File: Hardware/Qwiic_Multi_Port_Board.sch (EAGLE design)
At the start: 9 parts, among them J1 QWIIC_RIGHT_ANGLE, J2 QWIIC_RIGHT_ANGLE, J3 QWIIC_RIGHT_ANGLE, J4 QWIIC_RIGHT_ANGLE

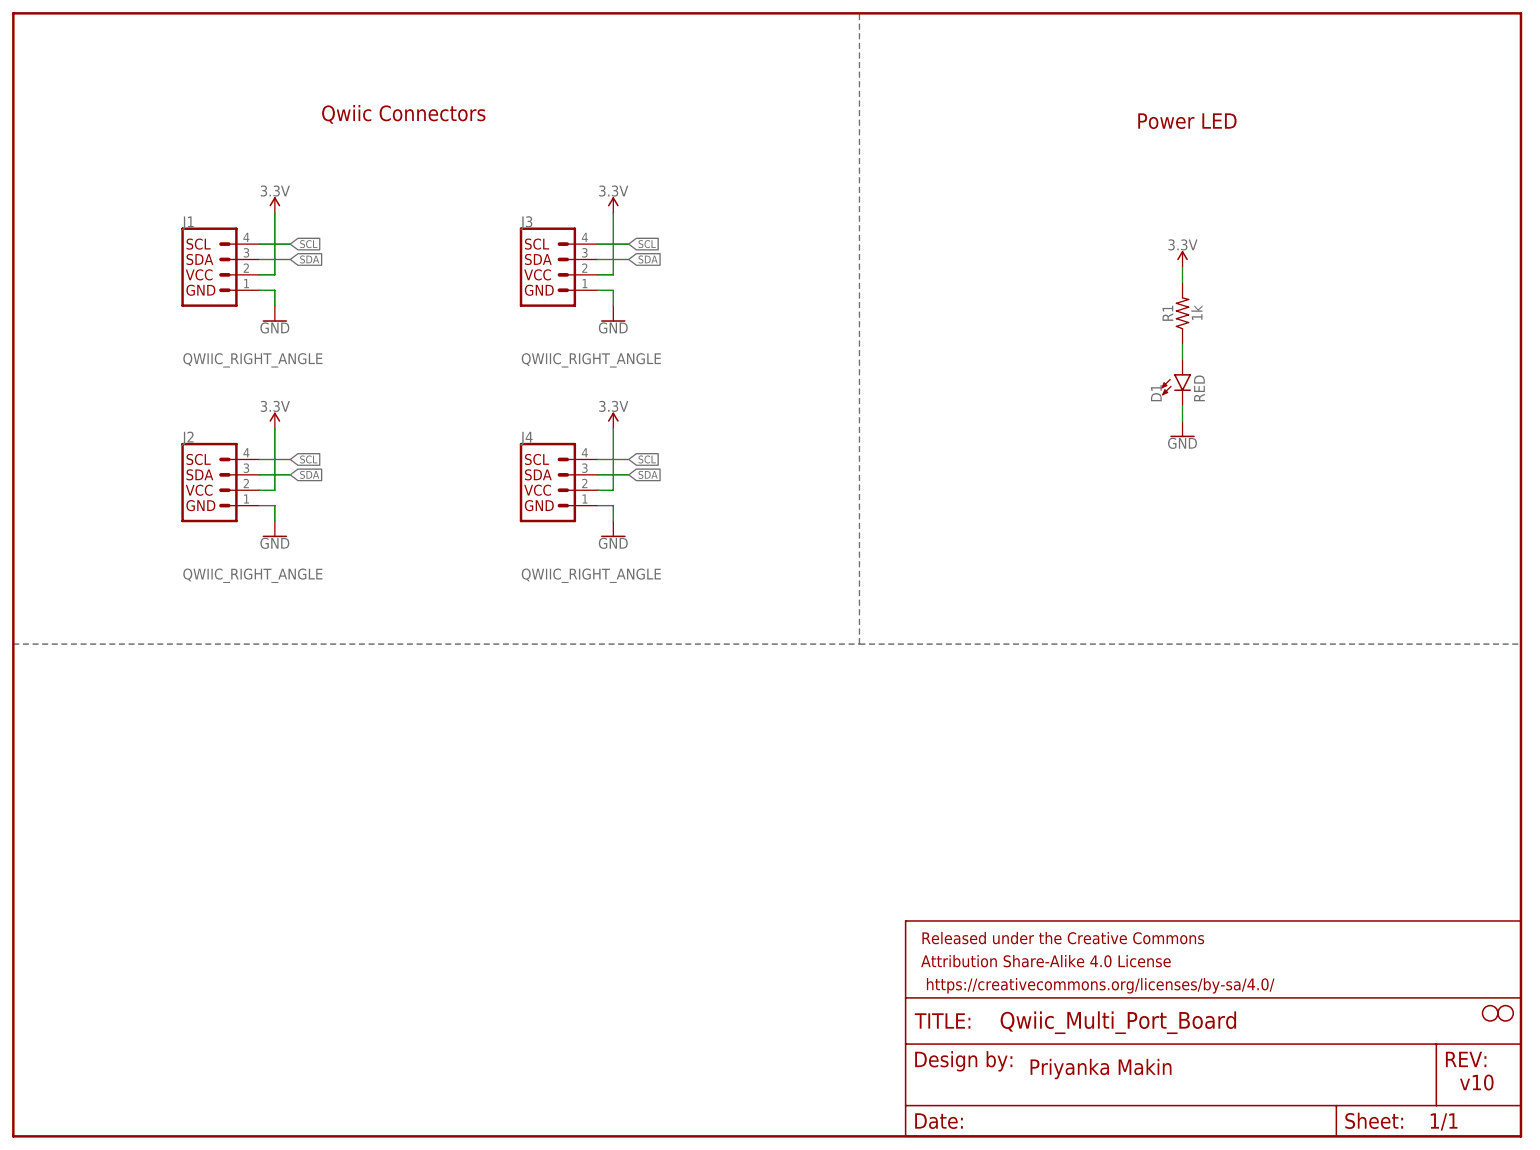
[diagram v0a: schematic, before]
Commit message: Multi Port: Design Review Changes
Added jumper on PWR LED
Added fiducials
Added OSHW, qwiic, SF logo as device on the schematic
Moved traces on top layer to avoid screws
Decided against:
un-populated I2C pullups -- not enough space
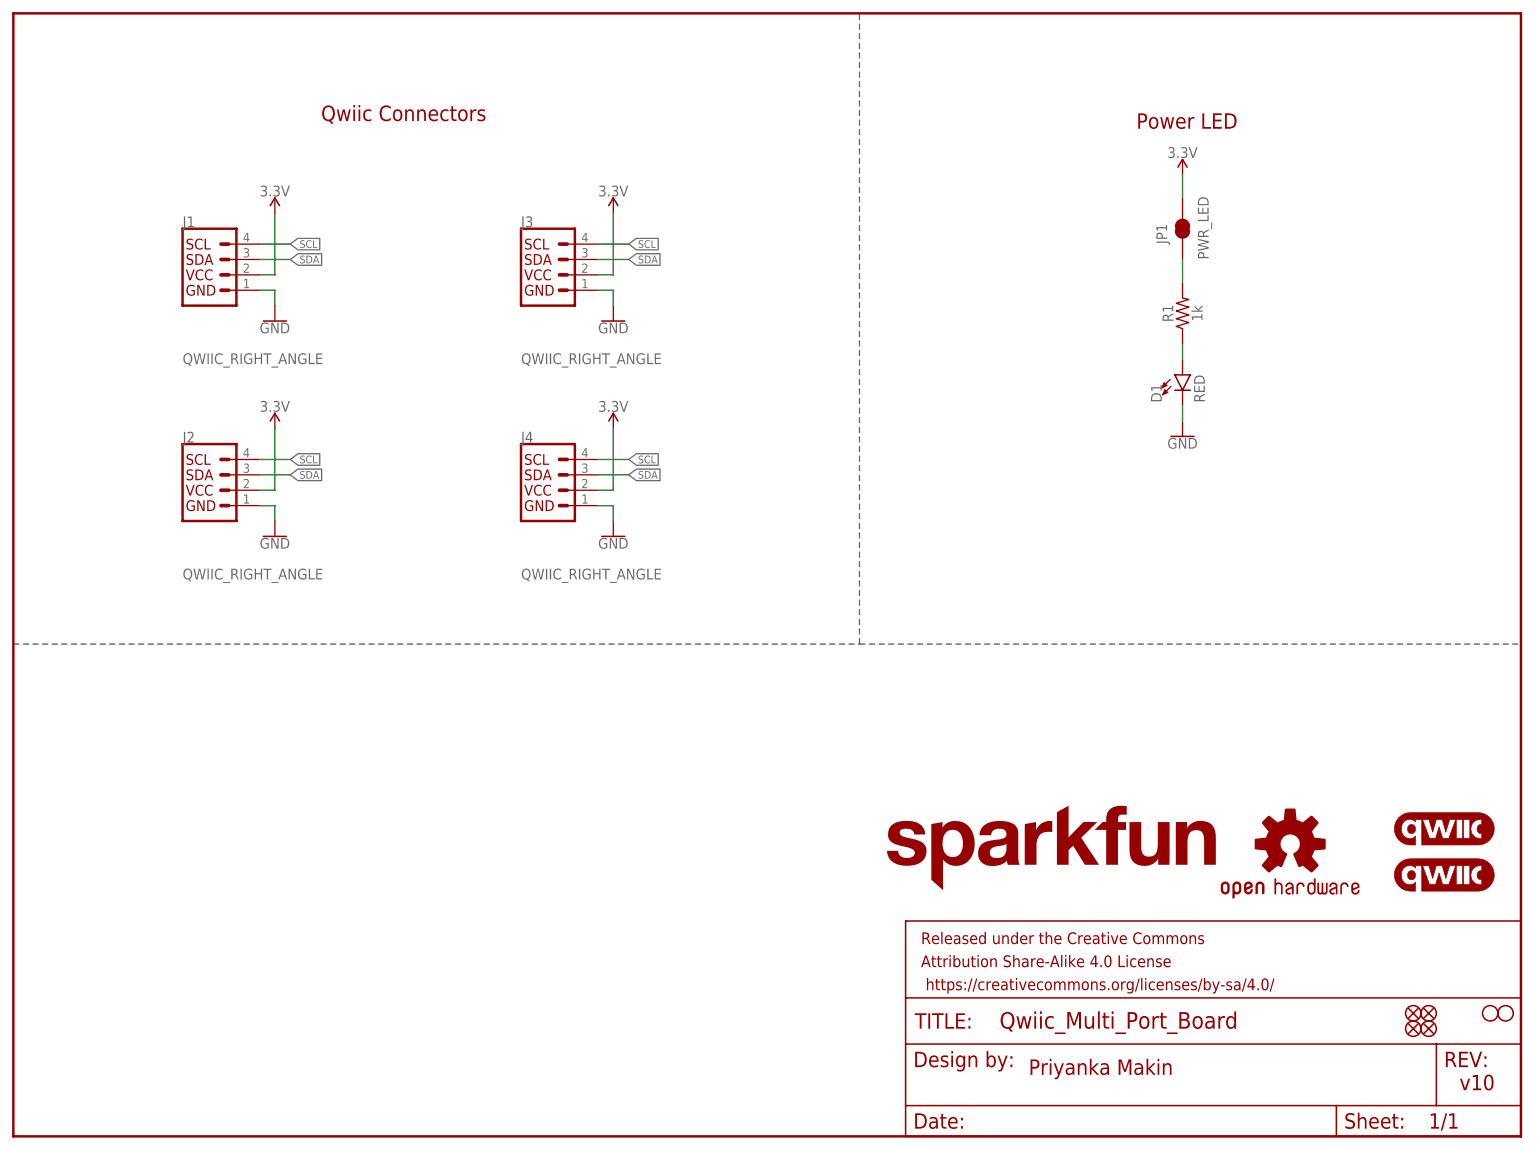
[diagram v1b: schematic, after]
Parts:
- added FD1, FD2, FD3, FD4: FIDUCIAL1X2, SparkFun-Aesthetics:FIDUCIAL1X2
- added JP1: PWR_LED, SparkFun-Jumpers:JUMPER-SMT_2_NC_TRACE_SILK
- added LOGO1, LOGO2: QWIIC_LOGO_5MM, SparkFun-Aesthetics:QWIIC_LOGO_5MM
- added LOGO3: OSHW-LOGOS, SparkFun-Aesthetics:OSHW-LOGOS
- added LOGO4: SFE_LOGO_NAME.2_INCH, SparkFun-Aesthetics:SFE_LOGO_NAME.2_INCH
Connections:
- new net N$2: JP1.1, R1.2
- net 3.3V: now also JP1.2; no longer R1.2

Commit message: Completed Engineering checklist
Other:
- note added: "Cut this jumper to disable the power LED"
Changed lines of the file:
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@@
 <grid distance="0.1" unitdist="inch" unit="inch" style="lines" multiple="1" display="no" altdistance="0.01" altunitdist="inch" altunit="inch"/>
 <layers>
-<layer number="1" name="Top" color="4" fill="1" visible="yes" active="no"/>
-<layer number="2" name="Route2" color="16" fill="1" visible="yes" active="no"/>
-<layer number="3" name="Route3" color="4" fill="3" visible="yes" active="no"/>
-<layer number="4" name="Route4" color="1" fill="4" visible="yes" active="no"/>
-<layer number="5" name="Route5" color="4" fill="4" visible="yes" active="no"/>
-<layer number="6" name="Route6" color="1" fill="8" visible="yes" active="no"/>
-<layer number="7" name="Route7" color="4" fill="8" visible="yes" active="no"/>
-<layer number="8" name="Route8" color="1" fill="2" visible="yes" active="no"/>
-<layer number="9" name="Route9" color="4" fill="2" visible="yes" active="no"/>
-<layer number="10" name="Route10" color="1" fill="7" visible="yes" active="no"/>
-<layer number="11" name="Route11" color="4" fill="7" visible="yes" active="no"/>
-<layer number="12" name="Route12" color="1" fill="5" visible="yes" active="no"/>
-<layer number="13" name="Route13" color="4" fill="5" visible="yes" active="no"/>
-<layer number="14" name="Route14" color="1" fill="6" visible="yes" active="no"/>
-<layer number="15" name="Route15" color="23" fill="1" visible="yes" active="no"/>
-<layer number="16" name="Bottom" color="1" fill="1" visible="yes" active="no"/>
-<layer number="17" name="Pads" color="2" fill="1" visible="yes" active="no"/>
-<layer number="18" name="Vias" color="2" fill="1" visible="yes" active="no"/>
-<layer number="19" name="Unrouted" color="6" fill="1" visible="yes" active="no"/>
-<layer number="20" name="Dimension" color="24" fill="1" visible="yes" active="no"/>
-<layer number="21" name="tPlace" color="16" fill="1" visible="yes" active="no"/>
-<layer number="22" name="bPlace" color="14" fill="1" visible="yes" active="no"/>
-<layer number="23" name="tOrigins" color="15" fill="1" visible="yes" active="no"/>
-<layer number="24" name="bOrigins" color="15" fill="1" visible="yes" active="no"/>
-<layer number="25" name="tNames" color="7" fill="1" visible="yes" active="no"/>
-<layer number="26" name="bNames" color="7" fill="1" visible="yes" active="no"/>
-<layer number="27" name="tValues" color="7" fill="1" visible="yes" active="no"/>
-<layer number="28" name="bValues" color="7" fill="1" visible="yes" active="no"/>
+<layer number="1" name="Top" color="4" fill="1" visible="no" active="no"/>
+<layer number="2" name="Route2" color="16" fill="1" visible="no" active="no"/>
+<layer number="3" name="Route3" color="4" fill="3" visible="no" active="no"/>
+<layer number="4" name="Route4" color="1" fill="4" visible="no" active="no"/>
+<layer number="5" name="Route5" color="4" fill="4" visible="no" active="no"/>
+<layer number="6" name="Route6" color="1" fill="8" visible="no" active="no"/>
+<layer number="7" name="Route7" color="4" fill="8" visible="no" active="no"/>
+<layer number="8" name="Route8" color="1" fill="2" visible="no" active="no"/>
+<layer number="9" name="Route9" color="4" fill="2" visible="no" active="no"/>
+<layer number="10" name="Route10" color="1" fill="7" visible="no" active="no"/>
+<layer number="11" name="Route11" color="4" fill="7" visible="no" active="no"/>
+<layer number="12" name="Route12" color="1" fill="5" visible="no" active="no"/>
+<layer number="13" name="Route13" color="4" fill="5" visible="no" active="no"/>
+<layer number="14" name="Route14" color="1" fill="6" visible="no" active="no"/>
+<layer number="15" name="Route15" color="23" fill="1" visible="no" active="no"/>
+<layer number="16" name="Bottom" color="1" fill="1" visible="no" active="no"/>
+<layer number="17" name="Pads" color="2" fill="1" visible="no" active="no"/>
+<layer number="18" name="Vias" color="2" fill="1" visible="no" active="no"/>
+<layer number="19" name="Unrouted" color="6" fill="1" visible="no" active="no"/>
+<layer number="20" name="Dimension" color="24" fill="1" visible="no" active="no"/>
+<layer number="21" name="tPlace" color="16" fill="1" visible="no" active="no"/>
+<layer number="22" name="bPlace" color="14" fill="1" visible="no" active="no"/>
+<layer number="23" name="tOrigins" color="15" fill="1" visible="no" active="no"/>
+<layer number="24" name="bOrigins" color="15" fill="1" visible="no" active="no"/>
+<layer number="25" name="tNames" color="7" fill="1" visible="no" active="no"/>
+<layer number="26" name="bNames" color="7" fill="1" visible="no" active="no"/>
+<layer number="27" name="tValues" color="7" fill="1" visible="no" active="no"/>
+<layer number="28" name="bValues" color="7" fill="1" visible="no" active="no"/>
 <layer number="29" name="tStop" color="7" fill="3" visible="no" active="no"/>
 <layer number="30" name="bStop" color="7" fill="6" visible="no" active="no"/>
@@
 <layer number="35" name="tGlue" color="7" fill="4" visible="no" active="no"/>
 <layer number="36" name="bGlue" color="7" fill="5" visible="no" active="no"/>
-<layer number="37" name="tTest" color="7" fill="1" visible="yes" active="no"/>
-<layer number="38" name="bTest" color="7" fill="1" visible="yes" active="no"/>
+<layer number="37" name="tTest" color="7" fill="1" visible="no" active="no"/>
+<layer number="38" name="bTest" color="7" fill="1" visible="no" active="no"/>
 <layer number="39" name="tKeepout" color="4" fill="11" visible="no" active="no"/>
 <layer number="40" name="bKeepout" color="1" fill="11" visible="no" active="no"/>
@@
 <layer number="44" name="Drills" color="7" fill="1" visible="no" active="no"/>
 <layer number="45" name="Holes" color="7" fill="1" visible="no" active="no"/>
-<layer number="46" name="Milling" color="3" fill="1" visible="yes" active="no"/>
-<layer number="47" name="Measures" color="7" fill="1" visible="yes" active="no"/>
-<layer number="48" name="Document" color="7" fill="1" visible="yes" active="no"/>
-<layer number="49" name="Reference" color="7" fill="1" visible="yes" active="no"/>
-<layer number="50" name="dxf" color="7" fill="1" visible="yes" active="no"/>
-<layer number="51" name="tDocu" color="6" fill="1" visible="yes" active="no"/>
-<layer number="52" name="bDocu" color="7" fill="1" visible="yes" active="no"/>
-<layer number="53" name="tGND_GNDA" color="7" fill="9" visible="yes" active="no"/>
-<layer number="54" name="bGND_GNDA" color="1" fill="9" visible="yes" active="no"/>
-<layer number="56" name="wert" color="7" fill="1" visible="yes" active="no"/>
-<layer number="57" name="tCAD" color="7" fill="1" visible="yes" active="no"/>
-<layer number="59" name="tCarbon" color="7" fill="1" visible="yes" active="no"/>
-<layer number="60" name="bCarbon" color="7" fill="1" visible="yes" active="no"/>
+<layer number="46" name="Milling" color="3" fill="1" visible="no" active="no"/>
+<layer number="47" name="Measures" color="7" fill="1" visible="no" active="no"/>
+<layer number="48" name="Document" color="7" fill="1" visible="no" active="no"/>
+<layer number="49" name="Reference" color="7" fill="1" visible="no" active="no"/>
+<layer number="50" name="dxf" color="7" fill="1" visible="no" active="no"/>
+<layer number="51" name="tDocu" color="6" fill="1" visible="no" active="no"/>
+<layer number="52" name="bDocu" color="7" fill="1" visible="no" active="no"/>
+<layer number="53" name="tGND_GNDA" color="7" fill="9" visible="no" active="no"/>
+<layer number="54" name="bGND_GNDA" color="1" fill="9" visible="no" active="no"/>
+<layer number="56" name="wert" color="7" fill="1" visible="no" active="no"/>
+<layer number="57" name="tCAD" color="7" fill="1" visible="no" active="no"/>
+<layer number="59" name="tCarbon" color="7" fill="1" visible="no" active="no"/>
+<layer number="60" name="bCarbon" color="7" fill="1" visible="no" active="no"/>
 <layer number="88" name="SimResults" color="9" fill="1" visible="yes" active="yes"/>
 <layer number="89" name="SimProbes" color="9" fill="1" visible="yes" active="yes"/>
@@
 <text x="185.42" y="166.37" size="2.54" layer="94" font="vector">Power LED</text>
 <wire x1="139.7" y1="81.28" x2="248.92" y2="81.28" width="0.2032" layer="97" style="longdash"/>
+<text x="203.2" y="144.78" size="2.54" layer="97" font="vector">Cut this jumper to
+disable the power LED</text>
 </plain>
 <instances>
@@
 </drawing>
 <compatibility>
+<note version="6.3" minversion="6.2.2" severity="warning">
+Since Version 6.2.2 text objects can contain more than one line,
+which will not be processed correctly with this version.
+</note>
 <note version="8.3" severity="warning">
 Since Version 8.3, EAGLE supports URNs for individual library
